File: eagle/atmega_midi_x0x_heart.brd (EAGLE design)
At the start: 100 x 80 mm, 33 parts, among them IC1 TL072P, J11_VCF_CUTOFF 22-23-2021, U1 ATMEGA328P_PDIP

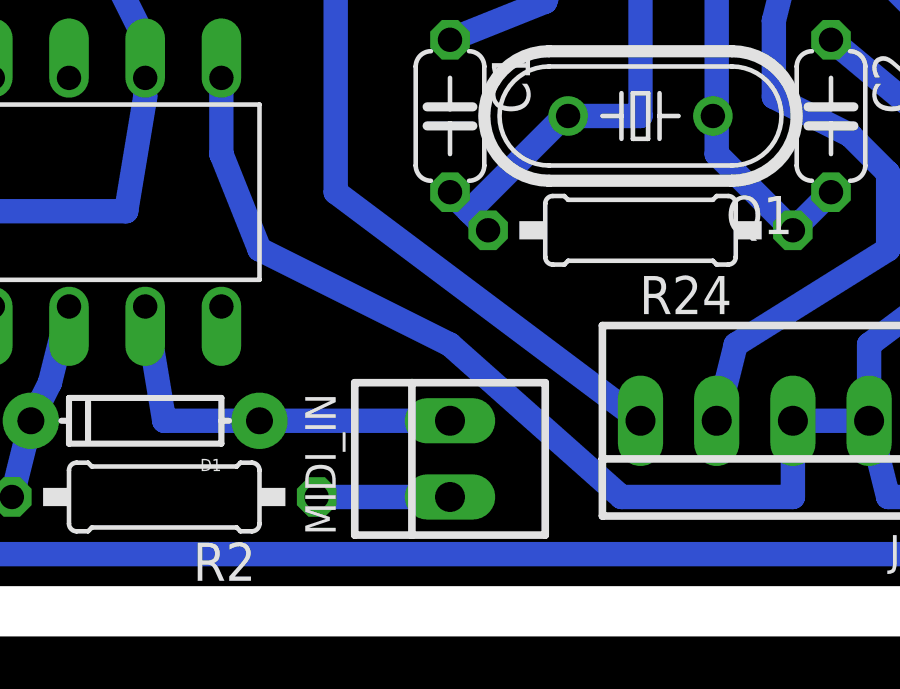
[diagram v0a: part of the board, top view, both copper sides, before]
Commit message: fixed touching trace
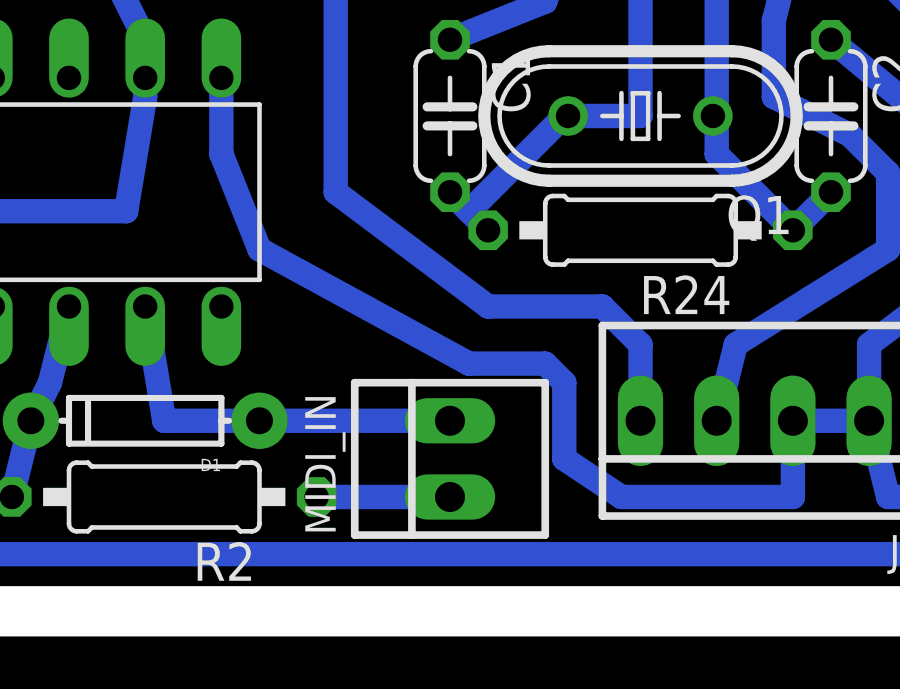
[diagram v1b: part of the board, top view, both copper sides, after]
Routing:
- net N$1: track 21.6 -> 23.4 mm
- net GND: track 245.3 -> 246.8 mm
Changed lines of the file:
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@@
 <contactref element="U1" pad="5"/>
 <wire x1="24.13" y1="21.59" x2="24.13" y2="30.48" width="0.8128" layer="16"/>
-<wire x1="34.29" y1="13.97" x2="24.13" y2="21.59" width="0.8128" layer="16"/>
+<wire x1="34.29" y1="13.97" x2="34.29" y2="16.51" width="0.8128" layer="16"/>
+<wire x1="34.29" y1="16.51" x2="33.02" y2="17.78" width="0.8128" layer="16"/>
+<wire x1="33.02" y1="17.78" x2="29.21" y2="17.78" width="0.8128" layer="16"/>
+<wire x1="29.21" y1="17.78" x2="24.13" y2="21.59" width="0.8128" layer="16"/>
 </signal>
 <signal name="N$9">
@@
 <wire x1="20.32" y1="22.86" x2="20.32" y2="25.4" width="0.8128" layer="16"/>
 <wire x1="21.59" y1="19.685" x2="20.32" y2="22.86" width="0.8128" layer="16"/>
-<wire x1="27.94" y1="16.51" x2="21.59" y2="19.685" width="0.8128" layer="16"/>
-<wire x1="33.655" y1="11.43" x2="27.94" y2="16.51" width="0.8128" layer="16"/>
+<wire x1="28.575" y1="15.875" x2="21.59" y2="19.685" width="0.8128" layer="16"/>
+<wire x1="33.655" y1="11.43" x2="31.75" y2="12.7" width="0.8128" layer="16"/>
+<wire x1="31.75" y1="12.7" x2="31.75" y2="15.24" width="0.8128" layer="16"/>
+<wire x1="31.75" y1="15.24" x2="31.115" y2="15.875" width="0.8128" layer="16"/>
+<wire x1="31.115" y1="15.875" x2="28.575" y2="15.875" width="0.8128" layer="16"/>
 <wire x1="39.37" y1="11.43" x2="33.655" y2="11.43" width="0.8128" layer="16"/>
 <wire x1="41.91" y1="13.97" x2="39.37" y2="13.97" width="0.8128" layer="16"/>

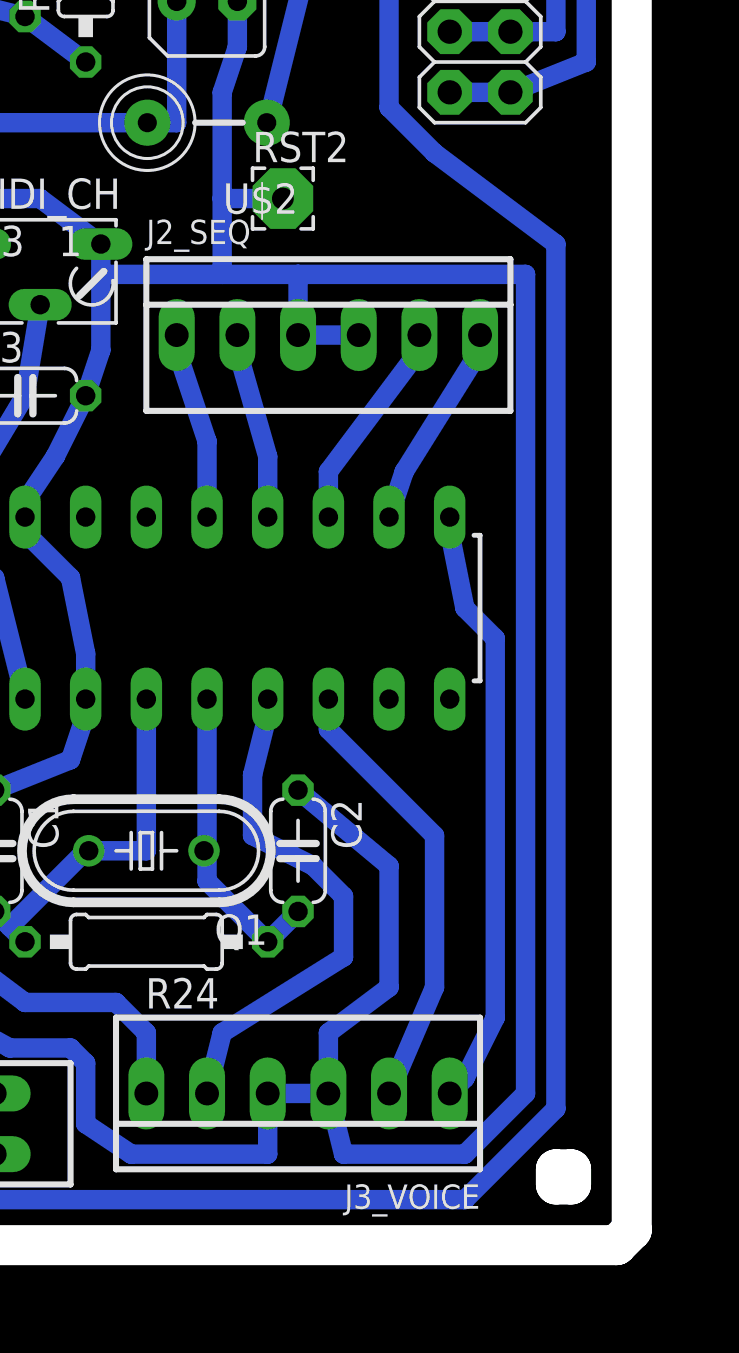
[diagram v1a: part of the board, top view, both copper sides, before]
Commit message: moved J2 away from midi channel trim
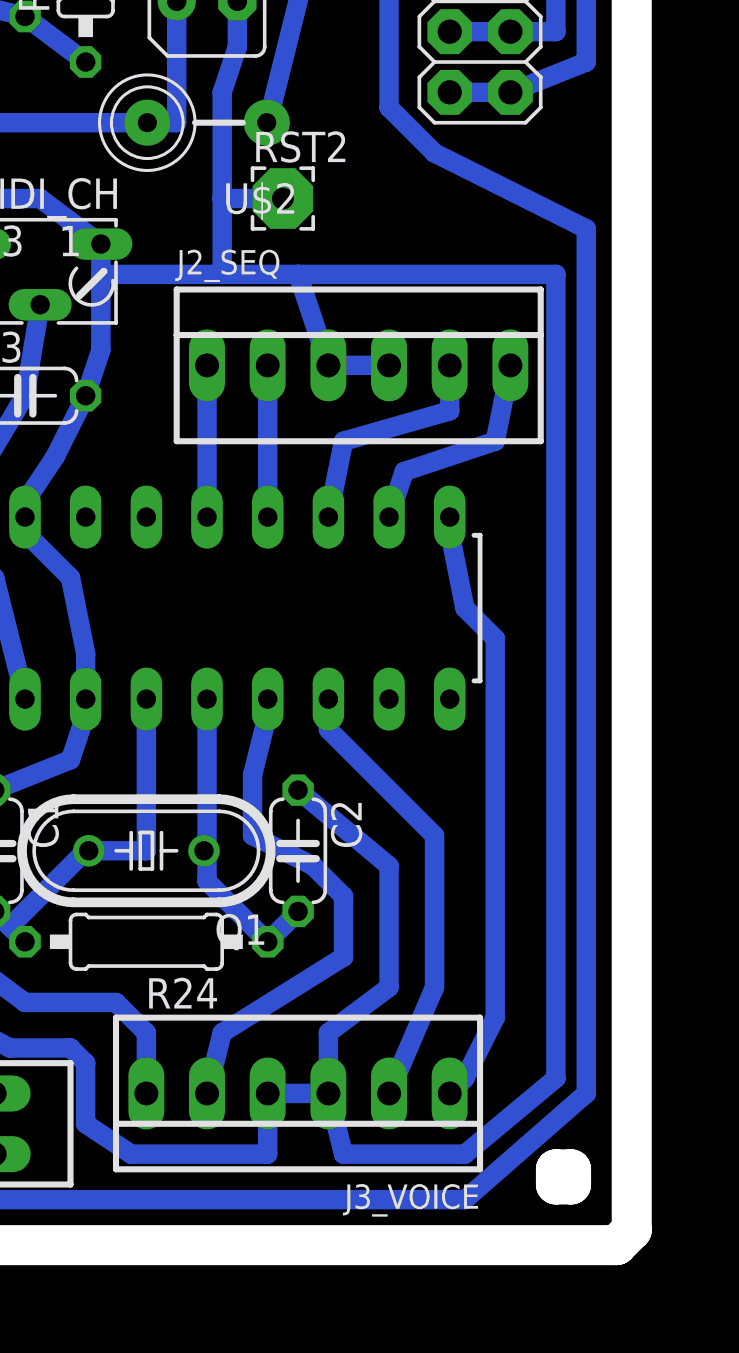
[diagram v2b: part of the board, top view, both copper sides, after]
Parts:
- moved J2_SEQ 1.80 mm to (43.2, 44.5)
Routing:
- net GND: track 246.8 -> 250.3 mm
- net +5V: track 194.4 -> 196.5 mm
- net N$18: track 7.83 -> 6.35 mm
- net N$20: track 7.80 -> 6.35 mm
- net N$21: track 8.89 -> 9.77 mm
- net N$23: track 8.63 -> 9.26 mm
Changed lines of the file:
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@@
 <attribute name="OC_FARNELL" value="1462926" x="36.83" y="69.85" size="1.778" layer="27" rot="R90" display="off"/>
 </element>
-<element name="J2_SEQ" library="con-molex" package="22-23-2061" value="" x="41.91" y="45.72">
-<attribute name="OC_NEWARK" value="27C1933" x="41.91" y="45.72" size="1.778" layer="27" display="off"/>
-<attribute name="MPN" value="22-23-2061" x="41.91" y="45.72" size="1.778" layer="27" display="off"/>
-<attribute name="MF" value="MOLEX" x="41.91" y="45.72" size="1.778" layer="27" display="off"/>
-<attribute name="OC_FARNELL" value="1462922" x="41.91" y="45.72" size="1.778" layer="27" display="off"/>
+<element name="J2_SEQ" library="con-molex" package="22-23-2061" value="" x="43.18" y="44.45">
+<attribute name="OC_NEWARK" value="27C1933" x="43.18" y="44.45" size="1.778" layer="27" display="off"/>
+<attribute name="MPN" value="22-23-2061" x="43.18" y="44.45" size="1.778" layer="27" display="off"/>
+<attribute name="MF" value="MOLEX" x="43.18" y="44.45" size="1.778" layer="27" display="off"/>
+<attribute name="OC_FARNELL" value="1462922" x="43.18" y="44.45" size="1.778" layer="27" display="off"/>
 </element>
 <element name="J3_VOICE" library="con-molex" package="22-23-2061" value="" x="40.64" y="13.97" rot="R180">
@@
 <wire x1="6.985" y1="15.24" x2="6.985" y2="23.495" width="0.8128" layer="16"/>
 <wire x1="47.625" y1="9.525" x2="12.7" y2="9.525" width="0.8128" layer="16"/>
-<wire x1="51.435" y1="13.335" x2="47.625" y2="9.525" width="0.8128" layer="16"/>
-<wire x1="51.435" y1="49.53" x2="51.435" y2="13.335" width="0.8128" layer="16"/>
-<wire x1="46.355" y1="53.34" x2="51.435" y2="49.53" width="0.8128" layer="16"/>
+<wire x1="52.705" y1="13.97" x2="47.625" y2="9.525" width="0.8128" layer="16"/>
+<wire x1="52.705" y1="50.165" x2="52.705" y2="13.97" width="0.8128" layer="16"/>
+<wire x1="46.355" y1="53.34" x2="52.705" y2="50.165" width="0.8128" layer="16"/>
 <wire x1="44.45" y1="55.245" x2="46.355" y2="53.34" width="0.8128" layer="16"/>
 <wire x1="44.45" y1="60.96" x2="44.45" y2="55.245" width="0.8128" layer="16"/>
@@
 <contactref element="J2_SEQ" pad="1"/>
 <contactref element="U1" pad="19"/>
-<wire x1="36.83" y1="41.275" x2="36.83" y2="38.1" width="0.8128" layer="16"/>
-<wire x1="35.56" y1="45.085" x2="36.83" y2="41.275" width="0.8128" layer="16"/>
-<wire x1="35.56" y1="45.72" x2="35.56" y2="45.085" width="0.8128" layer="16"/>
+<wire x1="36.83" y1="44.45" x2="36.83" y2="38.1" width="0.8128" layer="16"/>
 </signal>
 <signal name="N$20">
 <contactref element="U1" pad="18"/>
 <contactref element="J2_SEQ" pad="2"/>
-<wire x1="39.37" y1="40.64" x2="39.37" y2="38.1" width="0.8128" layer="16"/>
-<wire x1="38.1" y1="45.085" x2="39.37" y2="40.64" width="0.8128" layer="16"/>
-<wire x1="38.1" y1="45.72" x2="38.1" y2="45.085" width="0.8128" layer="16"/>
+<wire x1="39.37" y1="44.45" x2="39.37" y2="38.1" width="0.8128" layer="16"/>
 </signal>
 <signal name="N$21">
 <contactref element="J2_SEQ" pad="5"/>
 <contactref element="U1" pad="17"/>
-<wire x1="41.91" y1="40.005" x2="41.91" y2="38.1" width="0.8128" layer="16"/>
-<wire x1="45.72" y1="45.085" x2="41.91" y2="40.005" width="0.8128" layer="16"/>
-<wire x1="45.72" y1="45.72" x2="45.72" y2="45.085" width="0.8128" layer="16"/>
+<wire x1="42.545" y1="41.275" x2="41.91" y2="38.1" width="0.8128" layer="16"/>
+<wire x1="46.99" y1="42.545" x2="42.545" y2="41.275" width="0.8128" layer="16"/>
+<wire x1="46.99" y1="44.45" x2="46.99" y2="42.545" width="0.8128" layer="16"/>
 </signal>
 <signal name="N$23">
@@
 <contactref element="J2_SEQ" pad="6"/>
 <wire x1="45.085" y1="40.005" x2="44.45" y2="38.1" width="0.8128" layer="16"/>
-<wire x1="48.26" y1="45.085" x2="45.085" y2="40.005" width="0.8128" layer="16"/>
-<wire x1="48.26" y1="45.72" x2="48.26" y2="45.085" width="0.8128" layer="16"/>
+<wire x1="48.895" y1="41.275" x2="45.085" y2="40.005" width="0.8128" layer="16"/>
+<wire x1="49.53" y1="44.45" x2="48.895" y2="41.275" width="0.8128" layer="16"/>
 </signal>
 <signal name="N$1">
@@
 <wire x1="31.75" y1="29.845" x2="31.115" y2="27.94" width="0.8128" layer="16"/>
 <wire x1="31.75" y1="30.48" x2="31.75" y2="29.845" width="0.8128" layer="16"/>
-<wire x1="43.18" y1="45.72" x2="40.64" y2="45.72" width="0.8128" layer="16"/>
+<wire x1="44.45" y1="44.45" x2="41.91" y2="44.45" width="0.8128" layer="16"/>
 <wire x1="29.21" y1="38.735" x2="29.21" y2="38.1" width="0.8128" layer="16"/>
 <wire x1="30.48" y1="40.64" x2="29.21" y2="38.735" width="0.8128" layer="16"/>
@@
 <wire x1="32.385" y1="45.085" x2="32.385" y2="48.26" width="0.8128" layer="16"/>
 <wire x1="32.385" y1="48.26" x2="32.385" y2="49.53" width="0.8128" layer="16"/>
-<wire x1="40.64" y1="48.26" x2="40.64" y2="45.72" width="0.8128" layer="16"/>
+<wire x1="40.64" y1="48.26" x2="41.91" y2="44.45" width="0.8128" layer="16"/>
 <wire x1="32.385" y1="48.26" x2="37.465" y2="48.26" width="0.8128" layer="16"/>
 <wire x1="31.75" y1="32.385" x2="31.75" y2="30.48" width="0.8128" layer="16"/>
@@
 <wire x1="42.545" y1="11.43" x2="41.91" y2="13.97" width="0.8128" layer="16"/>
 <wire x1="47.625" y1="11.43" x2="42.545" y2="11.43" width="0.8128" layer="16"/>
-<wire x1="50.165" y1="13.97" x2="47.625" y2="11.43" width="0.8128" layer="16"/>
-<wire x1="50.165" y1="48.26" x2="50.165" y2="13.97" width="0.8128" layer="16"/>
-<wire x1="40.64" y1="48.26" x2="50.165" y2="48.26" width="0.8128" layer="16"/>
+<wire x1="51.435" y1="14.605" x2="47.625" y2="11.43" width="0.8128" layer="16"/>
+<wire x1="51.435" y1="48.26" x2="51.435" y2="14.605" width="0.8128" layer="16"/>
+<wire x1="40.64" y1="48.26" x2="51.435" y2="48.26" width="0.8128" layer="16"/>
 <contactref element="GATE_LED" pad="K"/>
 <wire x1="40.64" y1="48.26" x2="37.465" y2="48.26" width="0.8128" layer="16"/>

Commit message: brd tweaks
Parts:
- moved MIDI_CH 2.01 mm to (27.9, 48.9), turned to 90 degrees
- moved RST2 1.42 mm to (41.3, 50.8)
- moved C1 1.27 mm to (27.9, 25.4)
- moved C2 1.27 mm to (40.6, 25.4)
- moved Q1 1.27 mm to (34.3, 25.4)
- moved R24 1.27 mm to (34.3, 21.6)
- moved C5 0.64 mm to (36.8, 60.3)
- moved MIDI_IN 0.64 mm to (27.3, 12.7)
- moved U$2 0.63 mm to (36.8, 55.2)
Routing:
- net GND: track 250.3 -> 247.5 mm
- net +5V: track 196.5 -> 193.7 mm
- net N$4: track 15.2 -> 12.9 mm
- net N$1: track 23.4 -> 21.4 mm
- net N$19: track 9.73 -> 11.7 mm
- net N$10: track 18.7 -> 19.5 mm
- net N$8: track 4.45 -> 3.81 mm
- net N$3: track 13.4 -> 12.8 mm
- net N$11: track 16.4 -> 17.0 mm
- net N$12: track 14.5 -> 15.0 mm

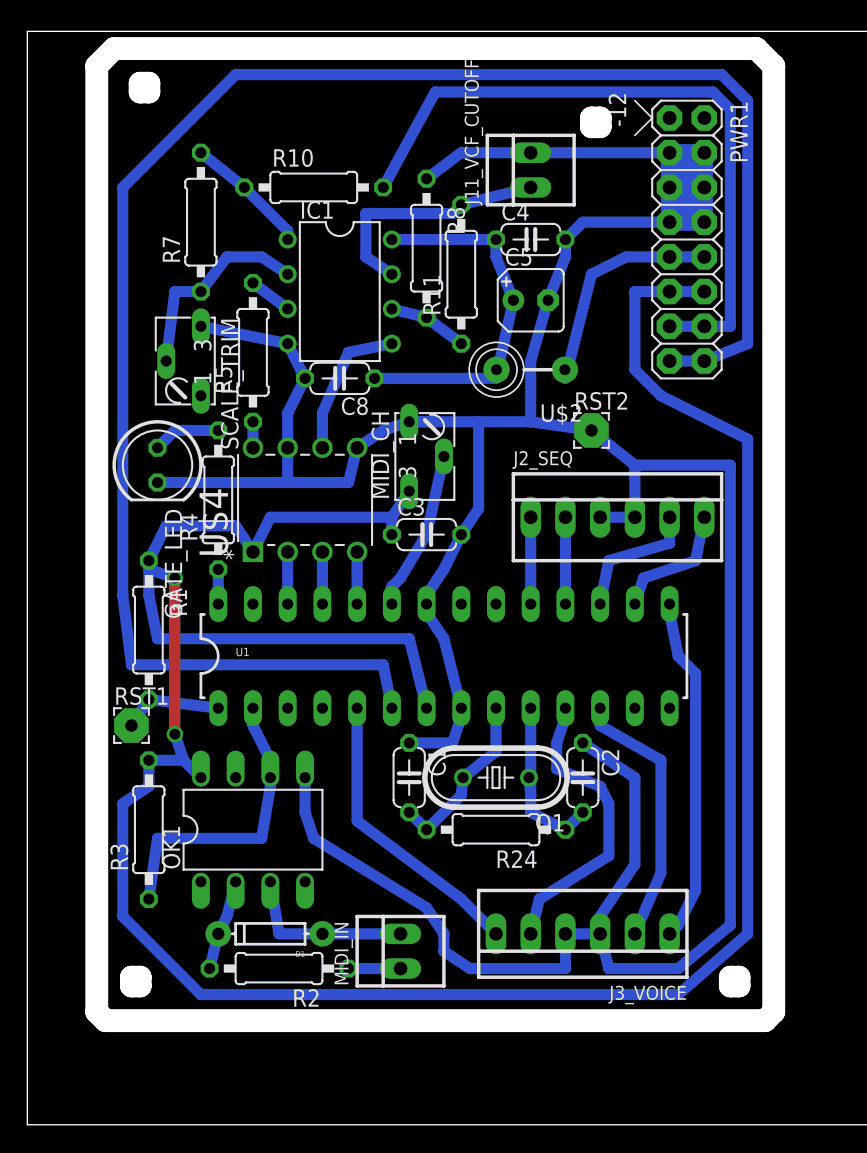
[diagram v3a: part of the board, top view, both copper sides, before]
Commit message: added vcf output resistor
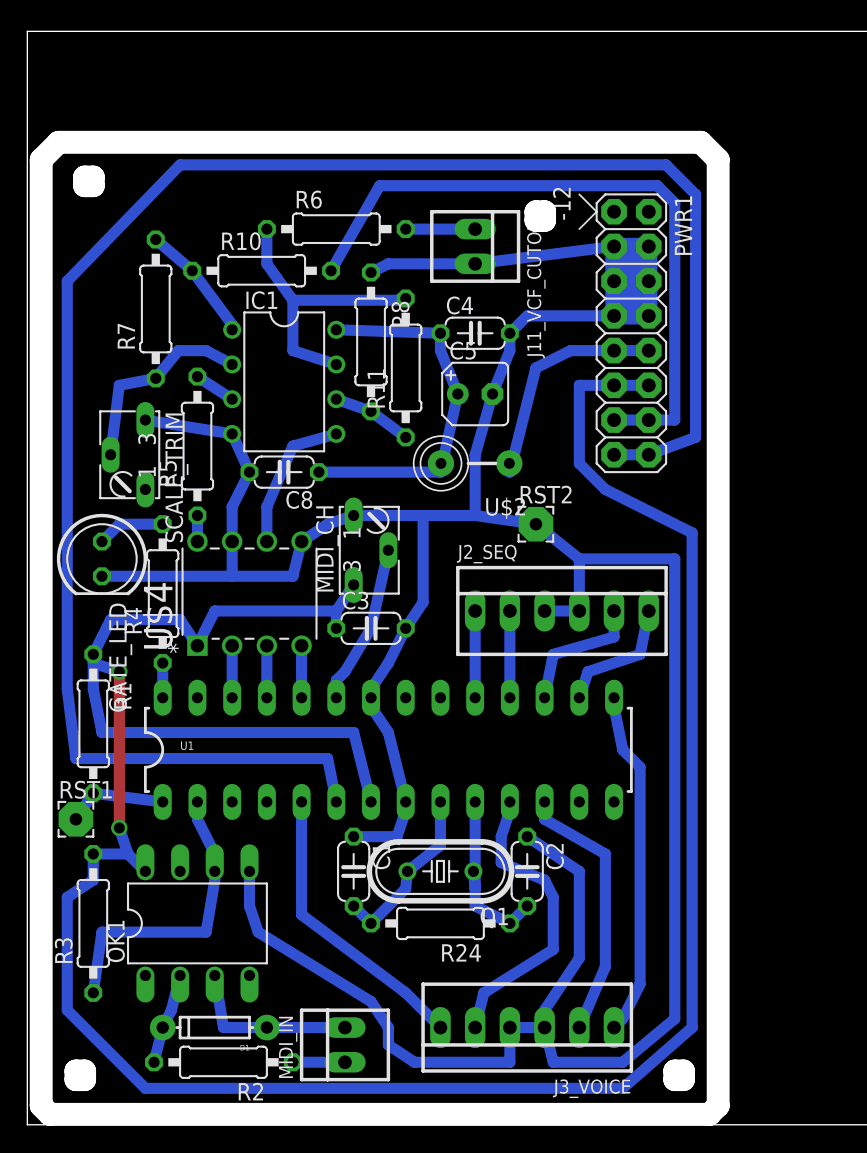
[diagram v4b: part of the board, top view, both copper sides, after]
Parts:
- added R6: 100k, rcl:0207/10
- moved C5 7.97 mm to (32.8, 53.5)
- moved J2_SEQ 7.97 mm to (39.1, 37.6)
- moved MIDI_CH 7.97 mm to (23.9, 42.0)
- moved PWR1 7.97 mm to (44.2, 60.5)
- moved R5 7.97 mm to (12.4, 49.7)
- moved R8 7.97 mm to (25.1, 57.3)
- moved SCALE_TRIM 7.97 mm to (8.64, 49.0)
- moved U$4 7.97 mm to (20.1, 42.7)
- moved D1 7.97 mm to (13.7, 7.11)
- moved OK1 7.97 mm to (12.4, 14.7)
- moved J3_VOICE 7.97 mm to (36.6, 7.11)
- moved R1 7.97 mm to (4.83, 29.3)
- moved R24 7.97 mm to (30.2, 14.7)
- moved R3 7.97 mm to (4.83, 14.7)
- moved RST1 7.97 mm to (3.56, 22.4)
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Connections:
- new net N$29: J11_VCF_CUTOFF.1, R6.2
- net N$17: now also R6.1; no longer J11_VCF_CUTOFF.1
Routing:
- net N$29: track 0.00 -> 5.08 mm
- net N$17: track 17.9 -> 21.1 mm
- net N$15: track 50.4 -> 49.6 mm
- net N$22: track 130.3 -> 131.1 mm
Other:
- outline, holes or cut-outs redrawn
